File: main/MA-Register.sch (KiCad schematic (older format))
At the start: 6 parts, among them U57 74LS245, U58 74LS245, U59 74LS173, U60 74LS173, U61 74LS173, U62 74LS173

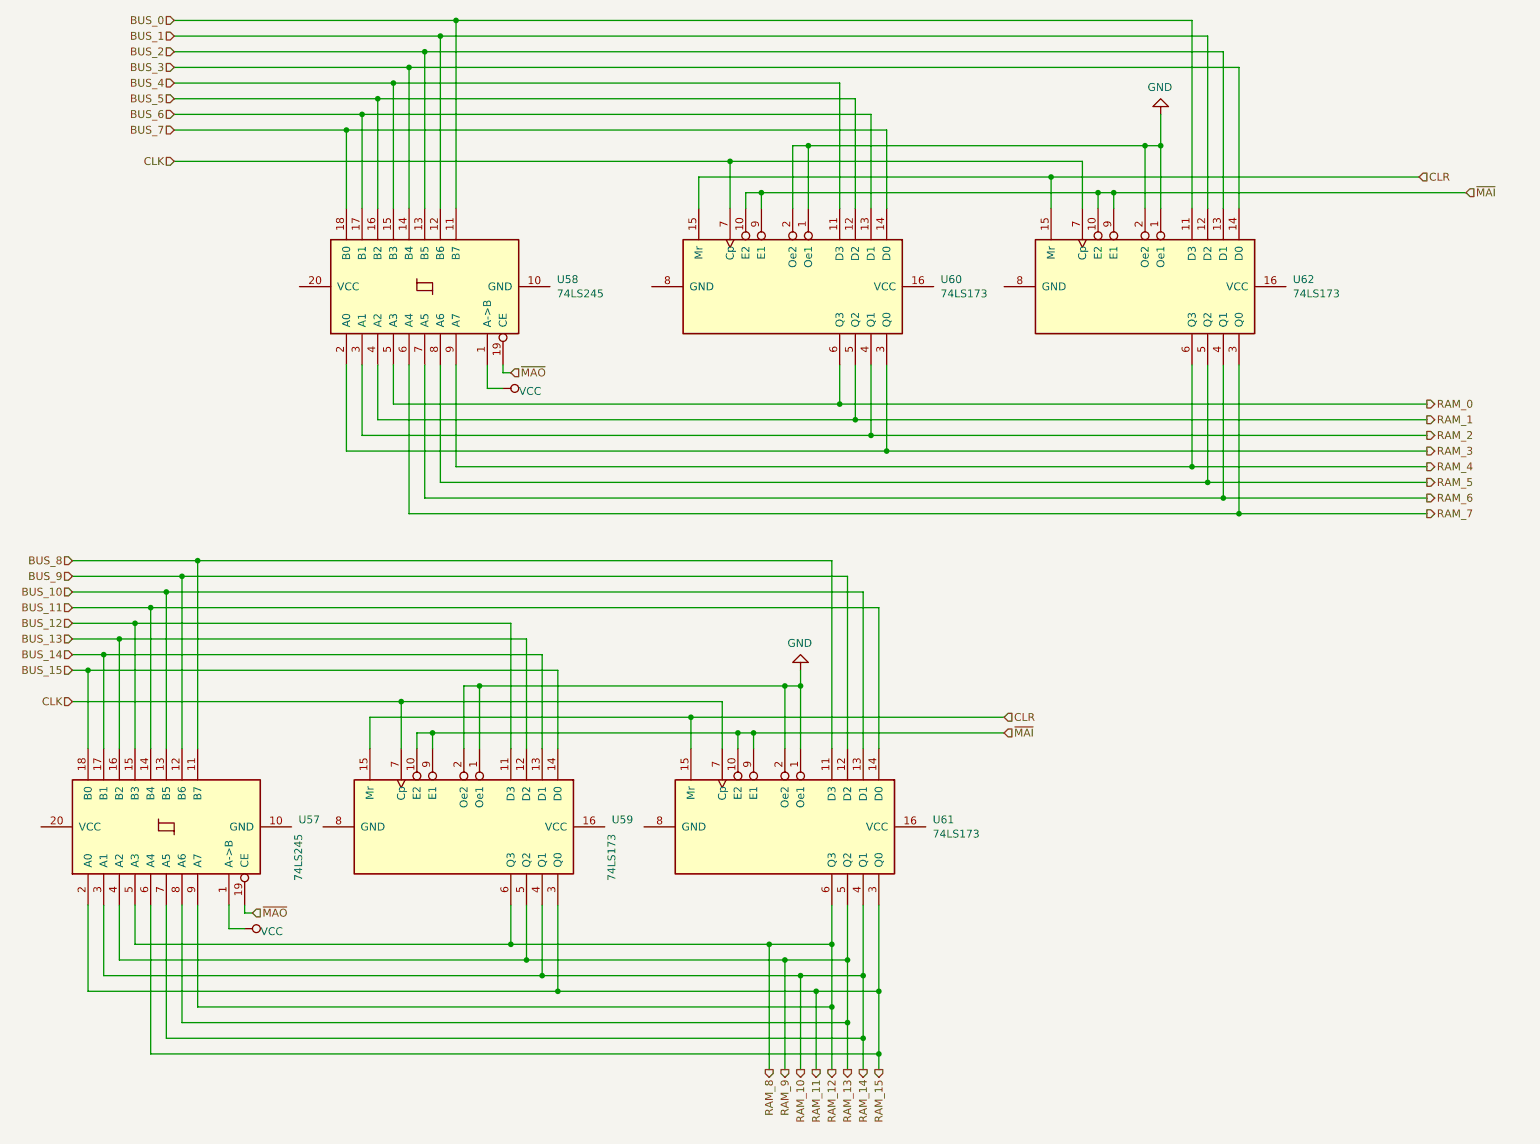
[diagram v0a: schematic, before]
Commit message: Replot main with symbols
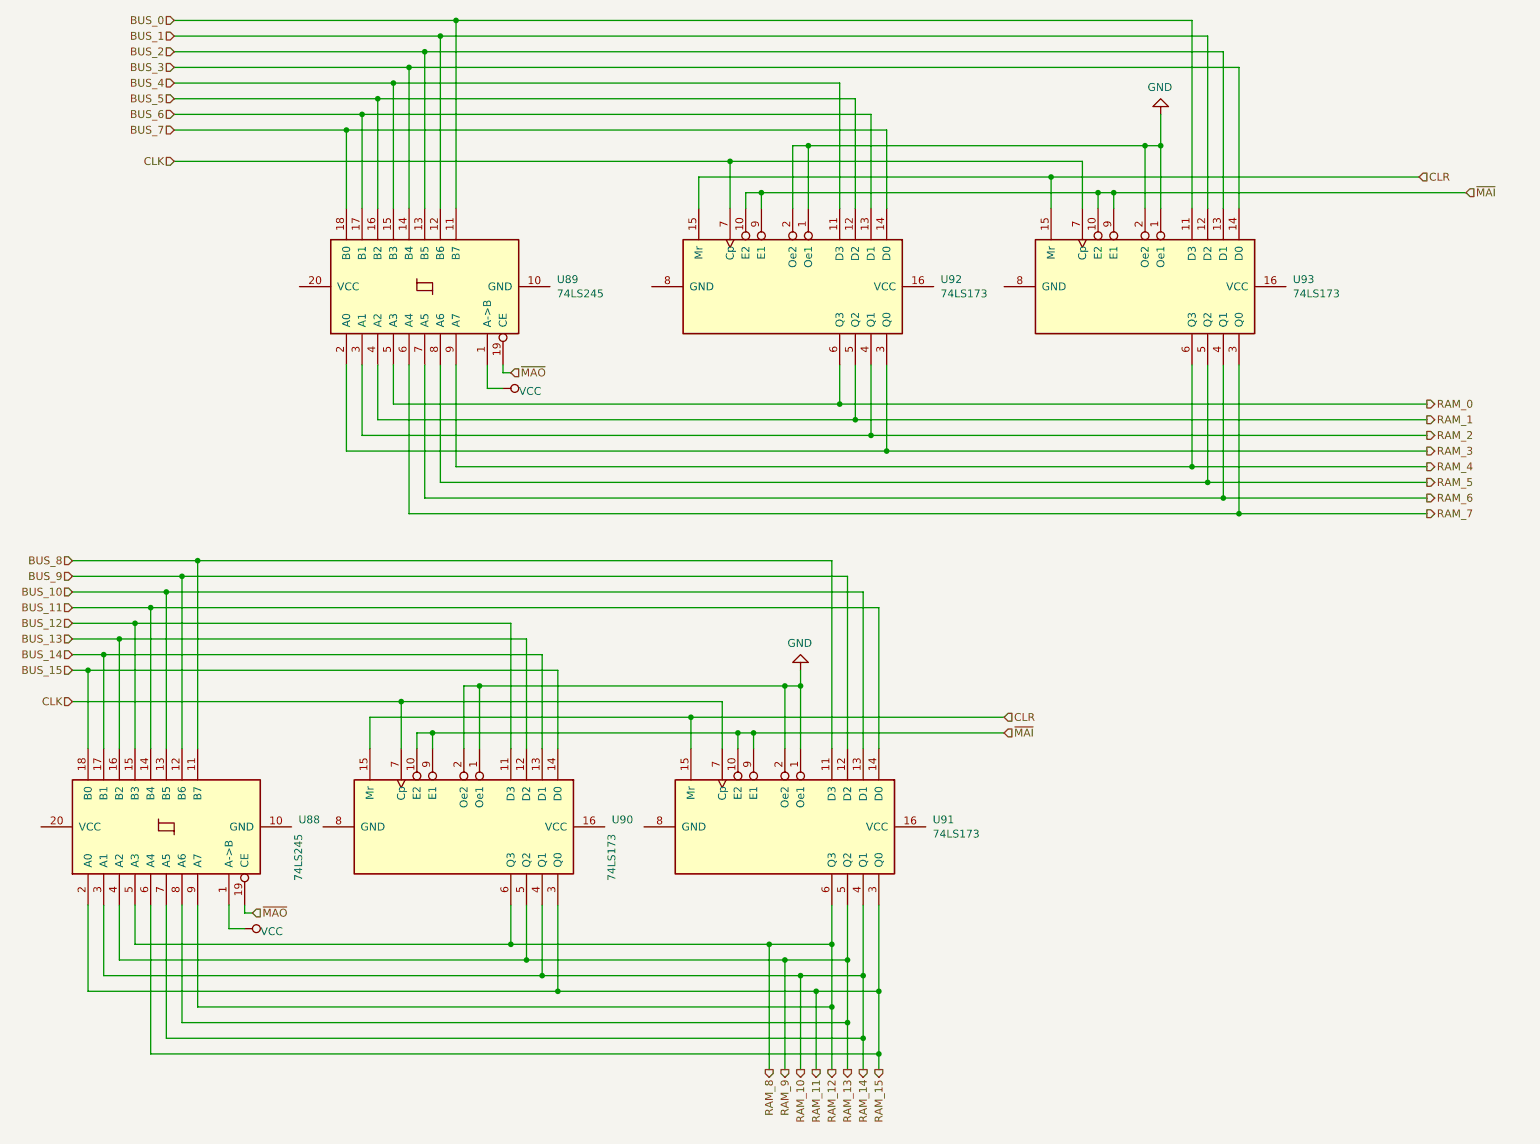
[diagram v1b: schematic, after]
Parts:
- renumbered U57 to U88, U58 to U89, U59 to U90, U61 to U91, U60 to U92, U62 to U93
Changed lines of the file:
@@
 Sheet 24 26
 Title "Memory Address Register"
-Date "2019-11-13"
+Date "2019-11-17"
 Rev "v1.0"
 Comp "Christopher Milan"
@@
 AR Path="/5DA98D6D/5DA9A5B3/5E64EBBE" Ref="U?"  Part="1"
 AR Path="/5DA9B7A7/5E64EBBE" Ref="U?"  Part="1"
-AR Path="/5E5B2276/5D807A05/5E64EBBE" Ref="U58"  Part="1"
-F 0 "U58" V 3246 1656 50  0000 R CNN
+AR Path="/5E5B2276/5D807A05/5E64EBBE" Ref="U89"  Part="1"
+F 0 "U89" V 3246 1656 50  0000 R CNN
 F 1 "74LS245" V 3155 1656 50  0000 R CNN
 F 2 "" H 3200 2500 50  0001 C CNN
@@
 AR Path="/5DA98D6D/5DA9A5B3/5E64EBEB" Ref="U?"  Part="1"
 AR Path="/5DA9B7A7/5E64EBEB" Ref="U?"  Part="1"
-AR Path="/5E5B2276/5D807A05/5E64EBEB" Ref="U62"  Part="1"
-F 0 "U62" V 7754 3444 50  0000 L CNN
+AR Path="/5E5B2276/5D807A05/5E64EBEB" Ref="U93"  Part="1"
+F 0 "U93" V 7754 3444 50  0000 L CNN
 F 1 "74LS173" V 7845 3444 50  0000 L CNN
 F 2 "" H 7800 2500 50  0001 C CNN
@@
 AR Path="/5DA98D6D/5DA9A5B3/5E64ECD6" Ref="U?"  Part="1"
 AR Path="/5DA9B7A7/5E64ECD6" Ref="U?"  Part="1"
-AR Path="/5E5B2276/5D807A05/5E64ECD6" Ref="U60"  Part="1"
-F 0 "U60" V 5504 3444 50  0000 L CNN
+AR Path="/5E5B2276/5D807A05/5E64ECD6" Ref="U92"  Part="1"
+F 0 "U92" V 5504 3444 50  0000 L CNN
 F 1 "74LS173" V 5595 3444 50  0000 L CNN
 F 2 "" H 5550 2500 50  0001 C CNN
@@
 AR Path="/5DA98D6D/5DA9A5B3/5E69CBF9" Ref="U?"  Part="1"
 AR Path="/5DA9B7A7/5E69CBF9" Ref="U?"  Part="1"
-AR Path="/5E5B2276/5D807A05/5E69CBF9" Ref="U59"  Part="1"
-F 0 "U59" V 3404 6894 50  0000 L CNN
+AR Path="/5E5B2276/5D807A05/5E69CBF9" Ref="U90"  Part="1"
+F 0 "U90" V 3404 6894 50  0000 L CNN
 F 1 "74LS173" H 3495 6894 50  0000 L CNN
 F 2 "" H 3450 5950 50  0001 C CNN
@@
 AR Path="/5DA98D6D/5DA9A5B3/5E69CB0E" Ref="U?"  Part="1"
 AR Path="/5DA9B7A7/5E69CB0E" Ref="U?"  Part="1"
-AR Path="/5E5B2276/5D807A05/5E69CB0E" Ref="U61"  Part="1"
-F 0 "U61" V 5454 6894 50  0000 L CNN
+AR Path="/5E5B2276/5D807A05/5E69CB0E" Ref="U91"  Part="1"
+F 0 "U91" V 5454 6894 50  0000 L CNN
 F 1 "74LS173" V 5545 6894 50  0000 L CNN
 F 2 "" H 5500 5950 50  0001 C CNN
@@
 AR Path="/5DA98D6D/5DA9A5B3/5E69CAE1" Ref="U?"  Part="1"
 AR Path="/5DA9B7A7/5E69CAE1" Ref="U?"  Part="1"
-AR Path="/5E5B2276/5D807A05/5E69CAE1" Ref="U57"  Part="1"
-F 0 "U57" V 1596 5106 50  0000 R CNN
+AR Path="/5E5B2276/5D807A05/5E69CAE1" Ref="U88"  Part="1"
+F 0 "U88" V 1596 5106 50  0000 R CNN
 F 1 "74LS245" H 1505 5106 50  0000 R CNN
 F 2 "" H 1550 5950 50  0001 C CNN

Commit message: Switch to using 74LS377 in place of two 74LS173
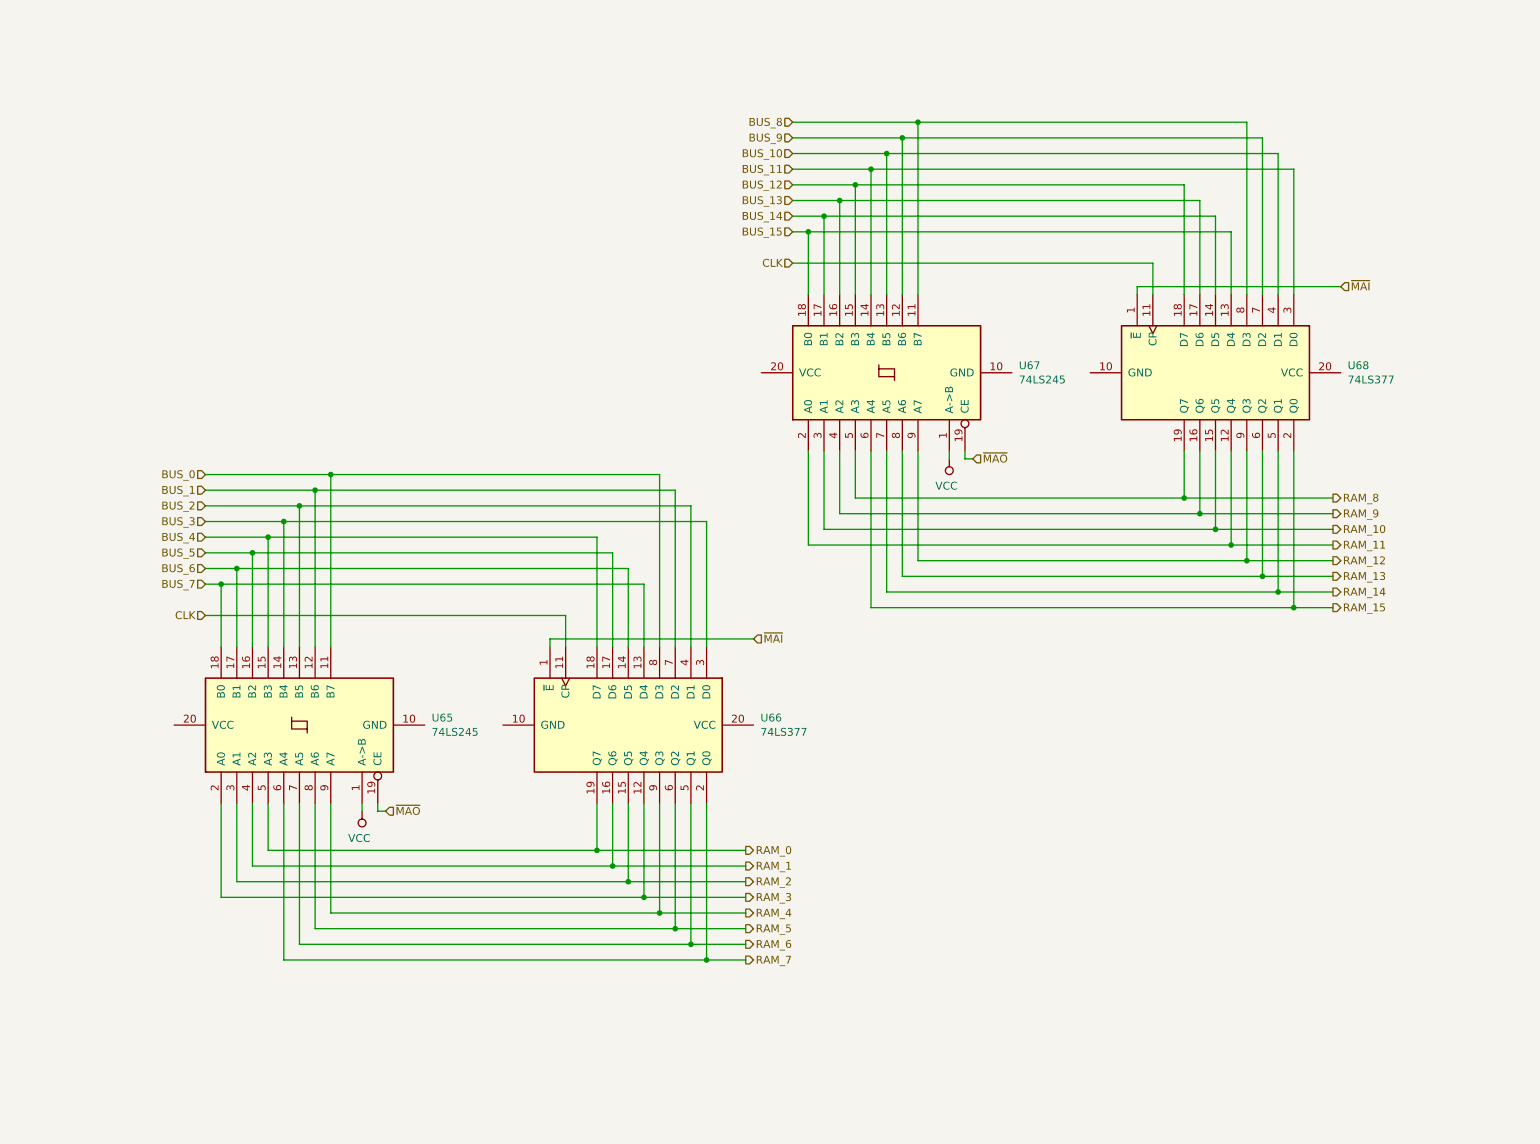
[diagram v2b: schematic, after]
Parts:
- removed U88, U89: 74LS245, symbol 74xx:74LS245
- removed U90, U91, U92, U93: 74LS173, symbol 74xx:74LS173
- added U65, U67: 74LS245, symbol 74xx:74LS245
- added U66, U68: 74LS377, symbol 74xx:74LS377
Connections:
- net BUS_0: now also U65.11 (B7), U66.8 (D3)
- net BUS_1: now also U65.12 (B6), U66.7 (D2)
- net BUS_10: now also U67.13 (B5), U68.4 (D1)
- net BUS_11: now also U67.14 (B4), U68.3 (D0)
- net BUS_12: now also U67.15 (B3), U68.18 (D7)
- net BUS_13: now also U67.16 (B2), U68.17 (D6)
- net BUS_14: now also U67.17 (B1), U68.14 (D5)
- net BUS_15: now also U67.18 (B0), U68.13 (D4)
- net BUS_2: now also U65.13 (B5), U66.4 (D1)
- net BUS_3: now also U65.14 (B4), U66.3 (D0)
- net BUS_4: now also U65.15 (B3), U66.18 (D7)
- net BUS_5: now also U65.16 (B2), U66.17 (D6)
- net BUS_6: now also U65.17 (B1), U66.14 (D5)
- net BUS_7: now also U65.18 (B0), U66.13 (D4)
- net BUS_8: now also U67.11 (B7), U68.8 (D3)
- net BUS_9: now also U67.12 (B6), U68.7 (D2)
- net CLK: now also U66.11 (CP), U68.11 (CP)
- net RAM_0: now also U65.5 (A3), U66.19 (Q7)
- net RAM_1: now also U65.4 (A2), U66.16 (Q6)
- net RAM_10: now also U67.3 (A1), U68.15 (Q5)
- net RAM_11: now also U67.2 (A0), U68.12 (Q4)
- net RAM_12: now also U67.9 (A7), U68.9 (Q3)
- net RAM_13: now also U67.8 (A6), U68.6 (Q2)
- net RAM_2: now also U65.3 (A1), U66.15 (Q5)
- net RAM_3: now also U65.2 (A0), U66.12 (Q4)
- net RAM_4: now also U65.9 (A7), U66.9 (Q3)
- net RAM_5: now also U65.8 (A6), U66.6 (Q2)
- net RAM_6: now also U65.7 (A5), U66.5 (Q1)
- net RAM_7: now also U65.6 (A4), U66.2 (Q0)
- net VCC: now also U65.1 (A->B), U67.1 (A->B)
- net ~MAI~: now also U66.1 (~E), U68.1 (~E)
- net ~MAO~: now also U65.19 (CE), U67.19 (CE)
- new net RAM_14: U67.7 (A5), U68.5 (Q1)
- new net RAM_15: U67.6 (A4), U68.2 (Q0)
- new net RAM_8: U67.5 (A3), U68.19 (Q7)
- new net RAM_9: U67.4 (A2), U68.16 (Q6)
